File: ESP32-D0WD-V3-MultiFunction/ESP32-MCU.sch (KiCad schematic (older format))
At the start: 31 parts, among them J201 Programming Header, SW201 RESET, U201 ESP32-D0WD-V3, U202 W25Q32JVSSIQ, Y201 40 Mhz +/- 10 ppm

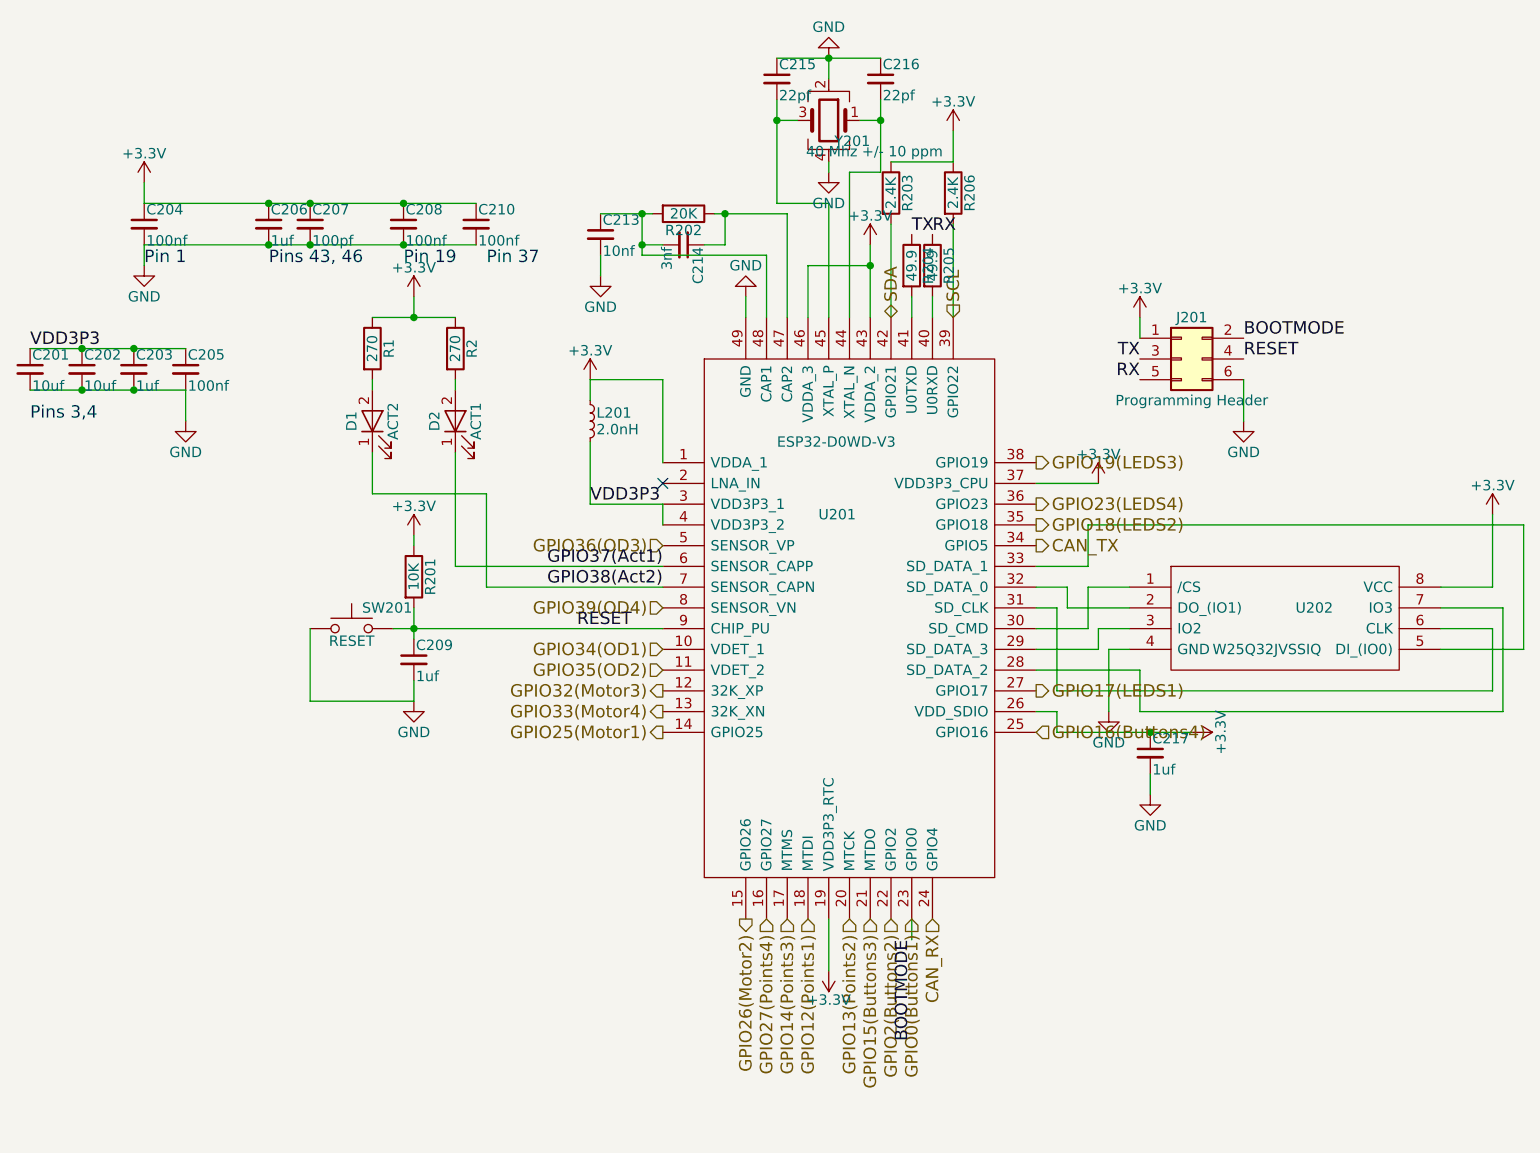
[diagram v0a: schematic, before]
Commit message: Fix incorrect I/O pin assignments.
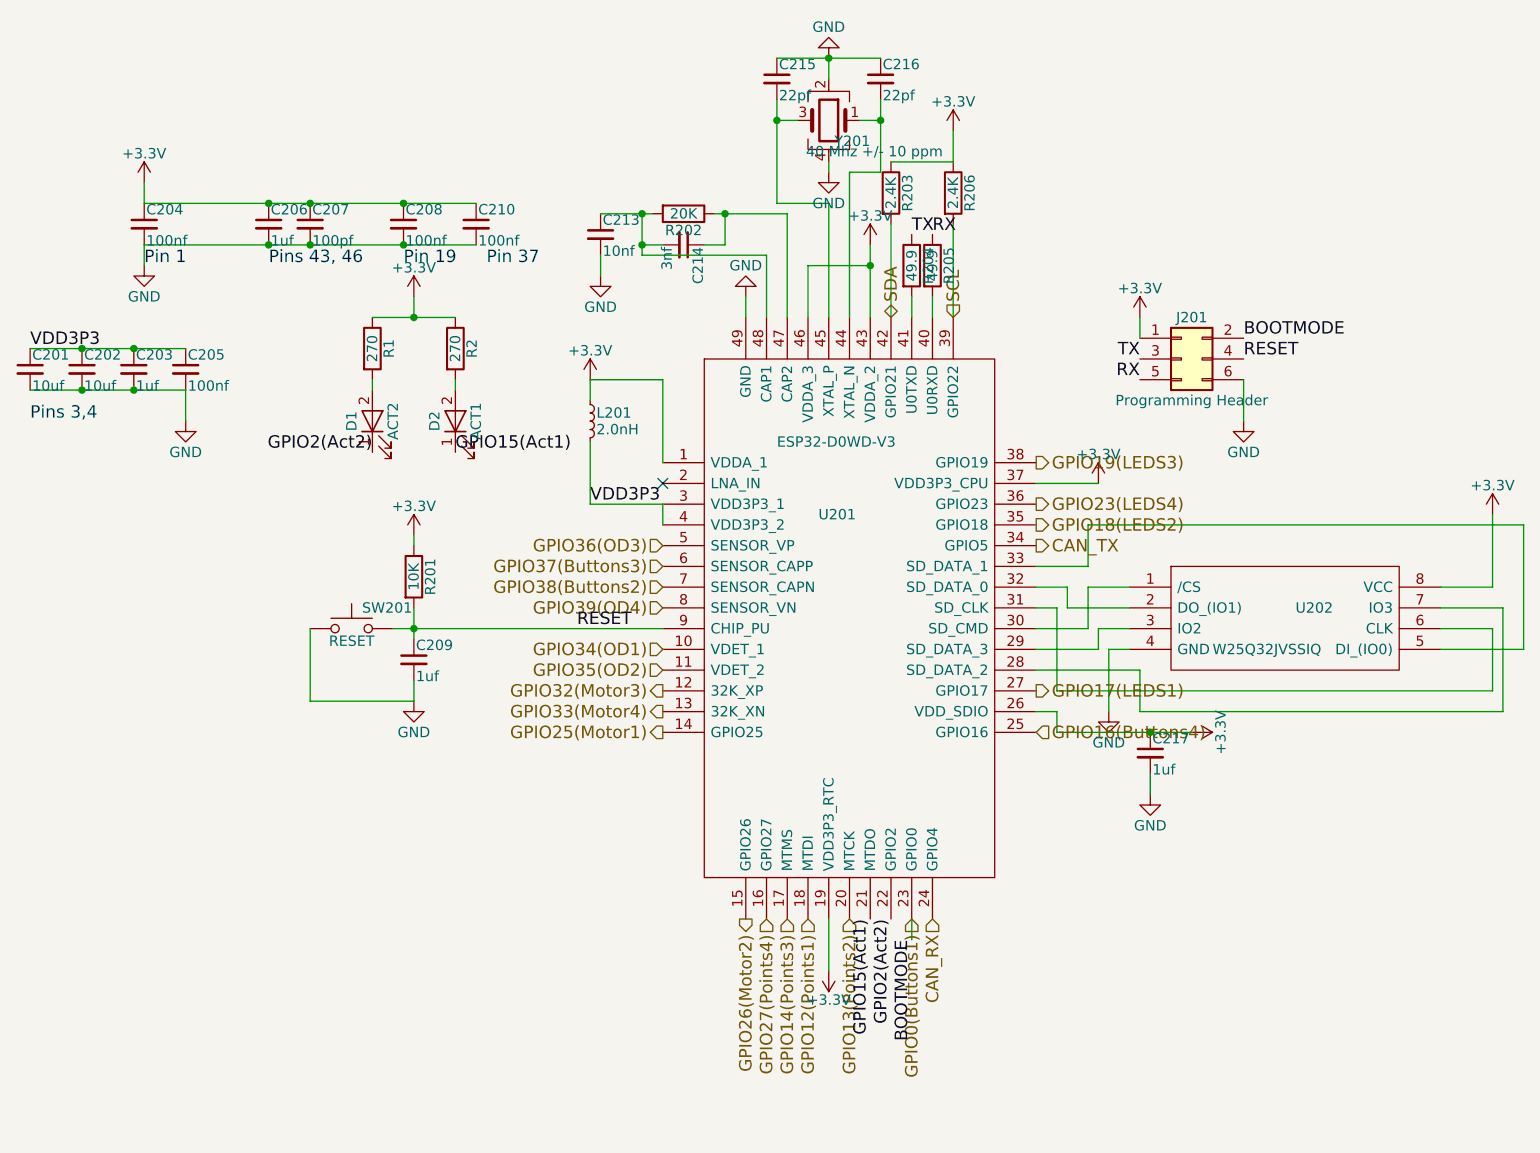
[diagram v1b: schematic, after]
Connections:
- net GPIO15(Buttons3) renamed GPIO15(Act1)
- net GPIO15(Act1): now also D2.1 (K)
- net GPIO2(Buttons2) renamed GPIO2(Act2)
- net GPIO2(Act2): now also D1.1 (K)
- net GPIO37(Act1) renamed GPIO37(Buttons3)
- net GPIO37(Buttons3): no longer D2.1 (K)
- net GPIO38(Act2) renamed GPIO38(Buttons2)
- net GPIO38(Buttons2): no longer D1.1 (K)
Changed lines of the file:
@@
 Text HLabel 6050 5400 3    60   Input ~ 0
 GPIO0(Buttons1)
-Text HLabel 5950 5400 3    60   Input ~ 0
-GPIO2(Buttons2)
+Text HLabel 4850 3800 0    60   Input ~ 0
+GPIO38(Buttons2)
 Text HLabel 5350 5400 3    60   Input ~ 0
 GPIO27(Points4)
@@
 Text HLabel 5450 5400 3    60   Input ~ 0
 GPIO14(Points3)
-Text HLabel 5850 5400 3    60   Input ~ 0
-GPIO15(Buttons3)
+Text HLabel 4850 3700 0    60   Input ~ 0
+GPIO37(Buttons3)
 Wire Wire Line
 	3650 4350 3150 4350
@@
 	6250 1750 6250 1600
 NoConn ~ 4850 3300
-Text Label 4850 3700 2    60   ~ 0
-GPIO37(Act1)
-Text Label 4850 3800 2    60   ~ 0
-GPIO38(Act2)
+Text Label 3850 3150 0    60   ~ 0
+GPIO15(Act1)
+Text Label 3450 3150 2    60   ~ 0
+GPIO2(Act2)
 $Comp
 L LED D2
@@
 Wire Wire Line
 	3450 2800 3450 2850
-Wire Wire Line
-	3850 3150 3850 3700
-Wire Wire Line
-	3850 3700 4850 3700
-Wire Wire Line
-	3450 3150 3450 3350
-Wire Wire Line
-	3450 3350 4000 3350
-Wire Wire Line
-	4000 3350 4000 3800
-Wire Wire Line
-	4000 3800 4850 3800
+Text Label 5950 5400 3    60   ~ 0
+GPIO2(Act2)
+Text Label 5850 5400 3    60   ~ 0
+GPIO15(Act1)
 $EndSCHEMATC

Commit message: Complete BOM for ESP32-D0WD-V3-MultiFunction.
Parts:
- C201, C202: Mouser Part Number (none) -> 187-CL21A106MQFNNNE
- C203, C206, C209, C217: Mouser Part Number (none) -> 80-C0402C101K8RAUTO
- C204, C205, C208, C210: Mouser Part Number (none) -> 710-885012105001
- C207: Mouser Part Number (none) -> 80-C0402C101K3RAUTO
- C213: Mouser Part Number (none) -> 81-GRM155R61E103KA1D
- C214: Mouser Part Number (none) -> 81-GRM1557U1A302JA1D
- R201: Mouser Part Number (none) -> 603-RC0402JR-1310KL
- R202: Mouser Part Number (none) -> 791-RMC10K203FTH
- R203, R206: Mouser Part Number (none) -> 71-CRCW06032K40JNEAC
- R204, R205: Mouser Part Number (none) -> 791-RMC1/16SK49R9FTH
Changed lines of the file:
@@
 encoding utf-8
 Sheet 2 8
-Title ""
+Title "ESP32 Multifunction Board"
 Date ""
-Rev ""
-Comp ""
+Rev "1.0"
+Comp "Deepwoods Software"
 Comment1 ""
 Comment2 ""
@@
 F 2 "Resistors_SMD:R_0402" V 6080 2250 50  0001 C CNN
 F 3 "" H 6150 2250 50  0001 C CNN
+F 4 "791-RMC1/16SK49R9FTH" V 6150 2250 60  0001 C CNN "Mouser Part Number"
 	1    6150 2250
 	1    0    0    -1
@@
 F 2 "Resistors_SMD:R_0402" V 5980 2250 50  0001 C CNN
 F 3 "" H 6050 2250 50  0001 C CNN
+F 4 "791-RMC1/16SK49R9FTH" V 6050 2250 60  0001 C CNN "Mouser Part Number"
 	1    6050 2250
 	1    0    0    -1
@@
 F 2 "Capacitors_SMD:C_0402" H 3650 4150 50  0001 C CNN
 F 3 "" H 3650 4150 50  0001 C CNN
+F 4 "80-C0402C101K8RAUTO" H 3650 4150 60  0001 C CNN "Mouser Part Number"
 	1    3650 4150
 	1    0    0    -1
@@
 F 2 "Resistors_SMD:R_0402" V 3580 3750 50  0001 C CNN
 F 3 "" H 3650 3750 50  0001 C CNN
+F 4 "603-RC0402JR-1310KL" V 3650 3750 60  0001 C CNN "Mouser Part Number"
 	1    3650 3750
 	1    0    0    -1
@@
 F 2 "Capacitors_SMD:C_0402" H 7200 4600 50  0001 C CNN
 F 3 "" H 7200 4600 50  0001 C CNN
+F 4 "80-C0402C101K8RAUTO" H 7200 4600 60  0001 C CNN "Mouser Part Number"
 	1    7200 4600
 	1    0    0    -1
@@
 F 2 "Resistors_SMD:R_0402" V 4880 2000 50  0001 C CNN
 F 3 "" H 4950 2000 50  0001 C CNN
+F 4 "791-RMC10K203FTH " V 4950 2000 60  0001 C CNN "Mouser Part Number"
 	1    4950 2000
 	0    1    1    0
@@
 F 2 "Capacitors_SMD:C_0402" H 4950 2150 50  0001 C CNN
 F 3 "" H 4950 2150 50  0001 C CNN
+F 4 "81-GRM1557U1A302JA1D" H 4950 2150 60  0001 C CNN "Mouser Part Number"
 	1    4950 2150
 	0    1    1    0
@@
 F 2 "Capacitors_SMD:C_0402" H 4550 2100 50  0001 C CNN
 F 3 "" H 4550 2100 50  0001 C CNN
+F 4 "81-GRM155R61E103KA1D" H 4550 2100 60  0001 C CNN "Mouser Part Number"
 	1    4550 2100
 	1    0    0    -1
@@
 F 2 "Capacitors_SMD:C_0805" H 1800 2750 50  0001 C CNN
 F 3 "" H 1800 2750 50  0001 C CNN
+F 4 "187-CL21A106MQFNNNE" H 1800 2750 60  0001 C CNN "Mouser Part Number"
 	1    1800 2750
 	1    0    0    -1
@@
 F 2 "Capacitors_SMD:C_0805" H 2050 2750 50  0001 C CNN
 F 3 "" H 2050 2750 50  0001 C CNN
+F 4 "187-CL21A106MQFNNNE" H 2050 2750 60  0001 C CNN "Mouser Part Number"
 	1    2050 2750
 	1    0    0    -1
@@
 F 2 "Capacitors_SMD:C_0402" H 2300 2750 50  0001 C CNN
 F 3 "" H 2300 2750 50  0001 C CNN
+F 4 "80-C0402C101K8RAUTO" H 2300 2750 60  0001 C CNN "Mouser Part Number"
 	1    2300 2750
 	1    0    0    -1
@@
 F 2 "Capacitors_SMD:C_0402" H 2550 2750 50  0001 C CNN
 F 3 "" H 2550 2750 50  0001 C CNN
+F 4 "710-885012105001" H 2550 2750 60  0001 C CNN "Mouser Part Number"
 	1    2550 2750
 	1    0    0    -1
@@
 F 2 "Capacitors_SMD:C_0402" H 2350 2050 50  0001 C CNN
 F 3 "" H 2350 2050 50  0001 C CNN
+F 4 "710-885012105001" H 2350 2050 60  0001 C CNN "Mouser Part Number"
 	1    2350 2050
 	1    0    0    -1
@@
 F 2 "Capacitors_SMD:C_0402" H 2950 2050 50  0001 C CNN
 F 3 "" H 2950 2050 50  0001 C CNN
+F 4 "80-C0402C101K8RAUTO" H 2950 2050 60  0001 C CNN "Mouser Part Number"
 	1    2950 2050
 	1    0    0    -1
@@
 F 2 "Capacitors_SMD:C_0402" H 3150 2050 50  0001 C CNN
 F 3 "" H 3150 2050 50  0001 C CNN
+F 4 "80-C0402C101K3RAUTO" H 3150 2050 60  0001 C CNN "Mouser Part Number"
 	1    3150 2050
 	1    0    0    -1
@@
 F 2 "Capacitors_SMD:C_0402" H 3600 2050 50  0001 C CNN
 F 3 "" H 3600 2050 50  0001 C CNN
+F 4 "710-885012105001" H 3600 2050 60  0001 C CNN "Mouser Part Number"
 	1    3600 2050
 	1    0    0    -1
@@
 F 2 "Capacitors_SMD:C_0402" H 3950 2050 50  0001 C CNN
 F 3 "" H 3950 2050 50  0001 C CNN
+F 4 "710-885012105001" H 3950 2050 60  0001 C CNN "Mouser Part Number"
 	1    3950 2050
 	1    0    0    -1
@@
 F 2 "Resistors_SMD:R_0402" V 5880 1900 50  0001 C CNN
 F 3 "" H 5950 1900 50  0001 C CNN
+F 4 "71-CRCW06032K40JNEAC" V 5950 1900 60  0001 C CNN "Mouser Part Number"
 	1    5950 1900
 	1    0    0    -1
@@
 F 2 "Resistors_SMD:R_0402" V 6180 1900 50  0001 C CNN
 F 3 "" H 6250 1900 50  0001 C CNN
+F 4 "71-CRCW06032K40JNEAC" V 6250 1900 60  0001 C CNN "Mouser Part Number"
 	1    6250 1900
 	1    0    0    -1
